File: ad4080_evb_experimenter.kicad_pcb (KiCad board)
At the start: 4 copper layers, 104.4 x 78.7 mm, 62 parts, among them J1 Conn_Coaxial, J2 Conn_Coaxial, J3 AudioJack2_Ground, J4 Conn_02x01, J5 Conn_02x01, J6 Conn_Coaxial, SW1 SW_Coded_SH-7050, U2 74LS163, U3 74HC04, X1 CXO_DIP8

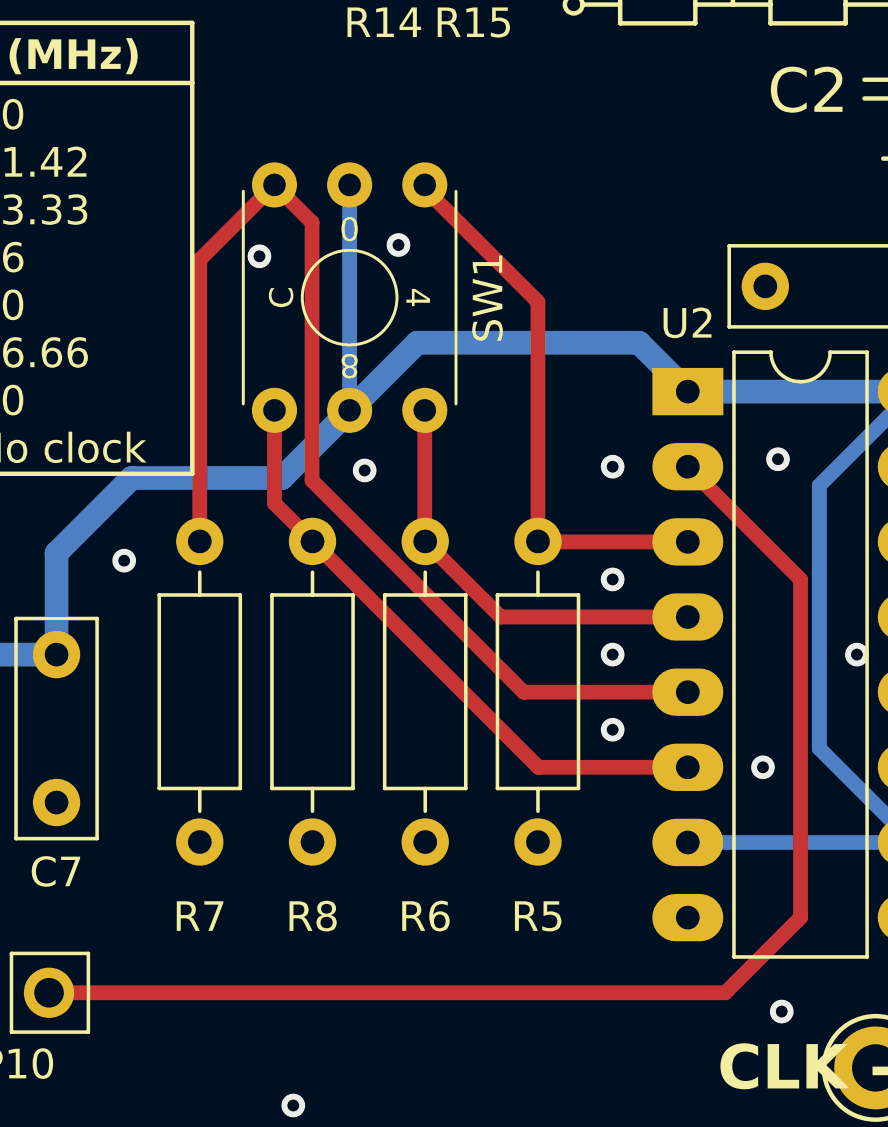
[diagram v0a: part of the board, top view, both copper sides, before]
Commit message: Fix swapped rotary encoder pins 2,8
Signed-off-by: Ioan Dragomir <ioan.dragomir@analog.com>
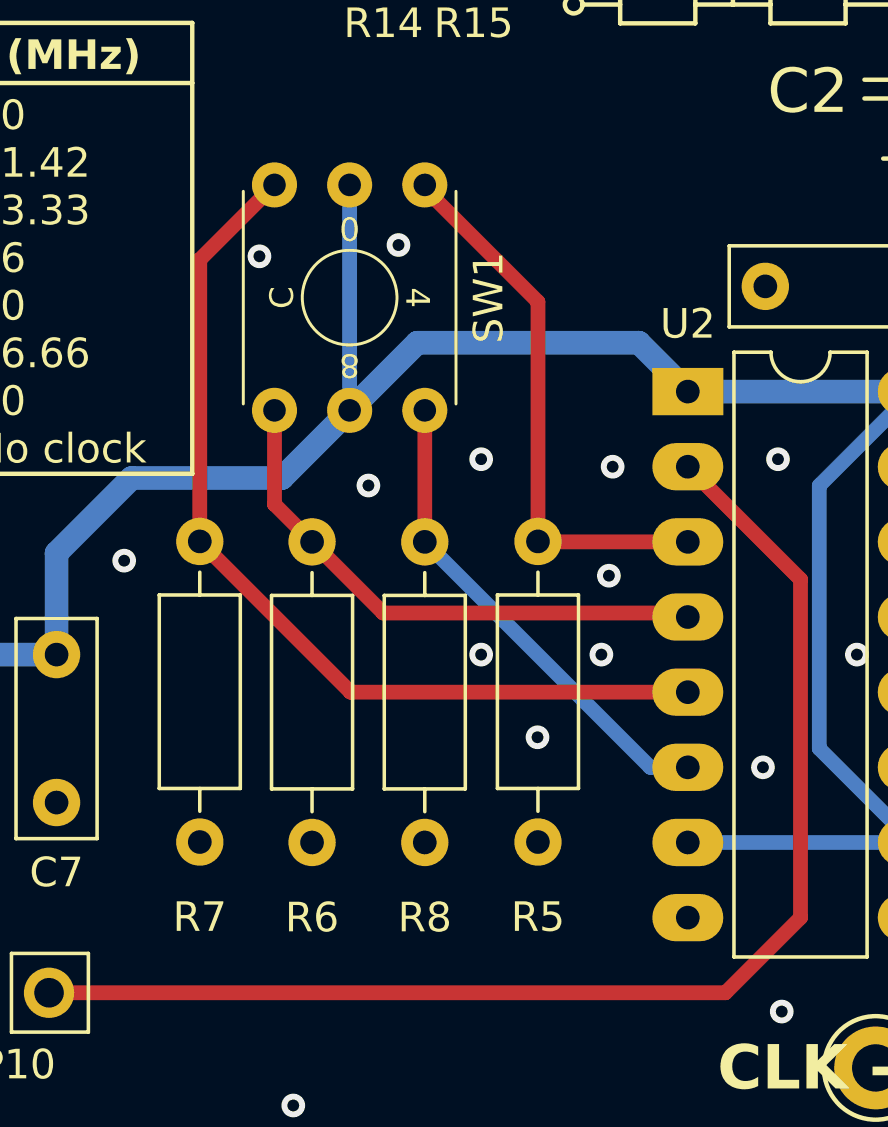
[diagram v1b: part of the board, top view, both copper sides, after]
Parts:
- moved R6 3.83 mm to (57.1, 100.3)
- moved R8 3.80 mm to (61.0, 100.3)
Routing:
- net Net-(U2-D2): track 39.3 -> 31.7 mm
- net Net-(U2-D1): track 14.3 -> 18.7 mm
- net Net-(U2-D3): track 20.8 -> 16.5 mm
- net GND: vias 78 -> 80

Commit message: Fix flipped opamp inputs
Signed-off-by: Ioan Dragomir <ioan.dragomir@analog.com>
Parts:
- moved C8 0.08 mm to (111.3, 71.8)
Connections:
- C8 pad 1: Net-(U1A-V-) -> Net-(U1A-V+)
- JP6 pad 2: Net-(U1A-V-) -> Net-(U1A-V+)
- JP6 pad 4: Net-(U1A-V-) -> Net-(U1A-V+)
- JP8 pad 2: Net-(U1A-V+) -> Net-(U1A-V-)
- JP8 pad 4: Net-(U1A-V+) -> Net-(U1A-V-)
- JP8 pad 6: Net-(U1A-V+) -> Net-(U1A-V-)
- R20 pad 2: Net-(U1A-V+) -> Net-(U1A-V-)
- R21 pad 1: Net-(U1A-V-) -> Net-(U1A-V+)
- R22 pad 1: Net-(U1A-V-) -> Net-(U1A-V+)
- R23 pad 1: Net-(U1A-V-) -> Net-(U1A-V+)
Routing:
- net Net-(U1A-V-): track 26.0 -> 22.1 mm
- net Net-(U1A-V+): track 23.3 -> 25.0 mm
- net GND: vias 80 -> 82

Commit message: Change to 2 layers
Signed-off-by: Ioan Dragomir <ioan.dragomir@analog.com>
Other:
- copper layers 4 -> 2

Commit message: Change test points to smaller Keystone Miniature
Signed-off-by: Ioan Dragomir <ioan.dragomir@analog.com>
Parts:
- TP1, TP2, TP3: footprint TestPoint:TestPoint_Plated_Hole_D3.0mm -> TestPoint:TestPoint_Keystone_5005-5009_Compact

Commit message: Add mounting holes, 3mm
Signed-off-by: Ioan Dragomir <ioan.dragomir@analog.com>
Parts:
- added H1: MountingHole_Pad, MountingHole:MountingHole_3mm_Pad, F.Cu at (47.9, 49.9)
- added H2: MountingHole_Pad, MountingHole:MountingHole_3mm_Pad, F.Cu at (47.9, 117.9)
- moved REF** 46.9 mm to (120.1, 60.8)
- moved JP10 10.4 mm to (56.1, 115.6)
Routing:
- net Net-(JP10-B): track 43.3 -> 32.9 mm
- net Net-(JP10-A): track 6.03 -> 14.8 mm
